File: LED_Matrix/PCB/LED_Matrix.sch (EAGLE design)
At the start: 8 parts, among them U1 ATTINY48, U2 ULN2803AFWG

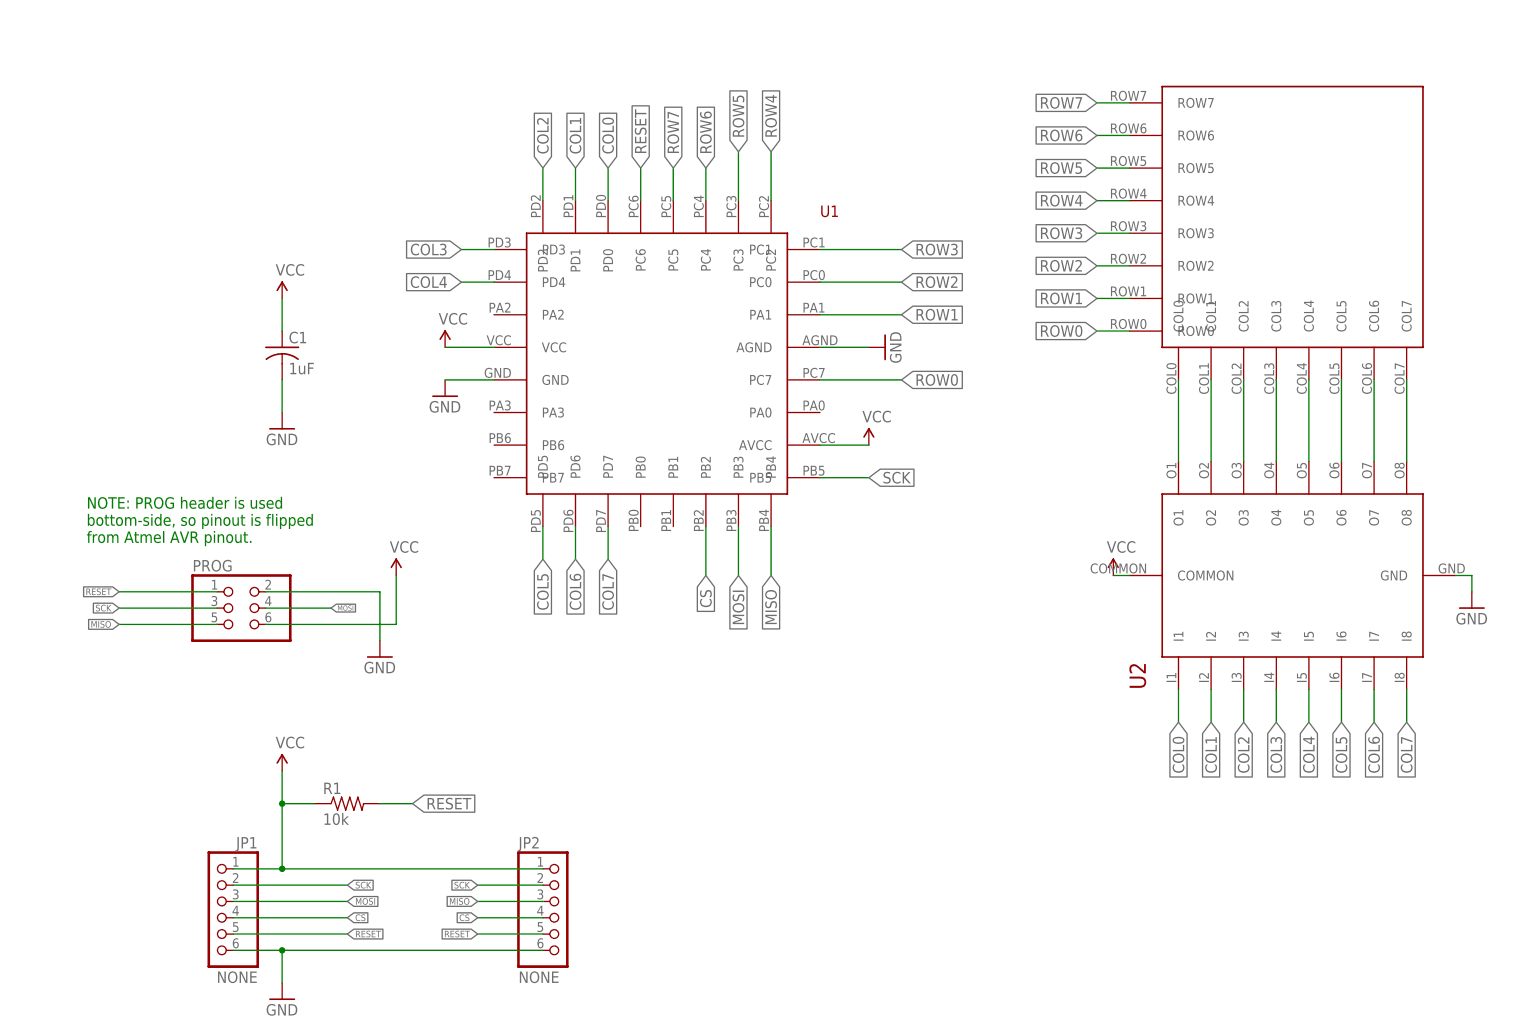
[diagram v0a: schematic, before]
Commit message: matrix - Rev-01b - Adjust size, mouting holes, split matrix connector.  No routing changes.
Dimensionsional, mounting, silkscreen and schematic changes.  (actually - there
was one very minor routing adjustment where a DRC check failed).

Changes:
    - Board was 1260x1260mils: changed to correct 1250x1250, which is the size
      of the LED matrix.
    - Mouting holes where 1010 mils apart, and still would hit the matrix
      headers with #4 screws.  Rather than do the correct 1000mils, went to
      1050 mils, which allow us only of one pair of mounting pins at a time.
      This is good because it allows all boards in a chain to use exactly two
      mounting holes.  Holes are now also labeled on the silkscreen.
    - Split LED matrix connector so that the BOM can have correct reference
      designator linkages.
    - Changed JP1/2 to more correct J/P designations
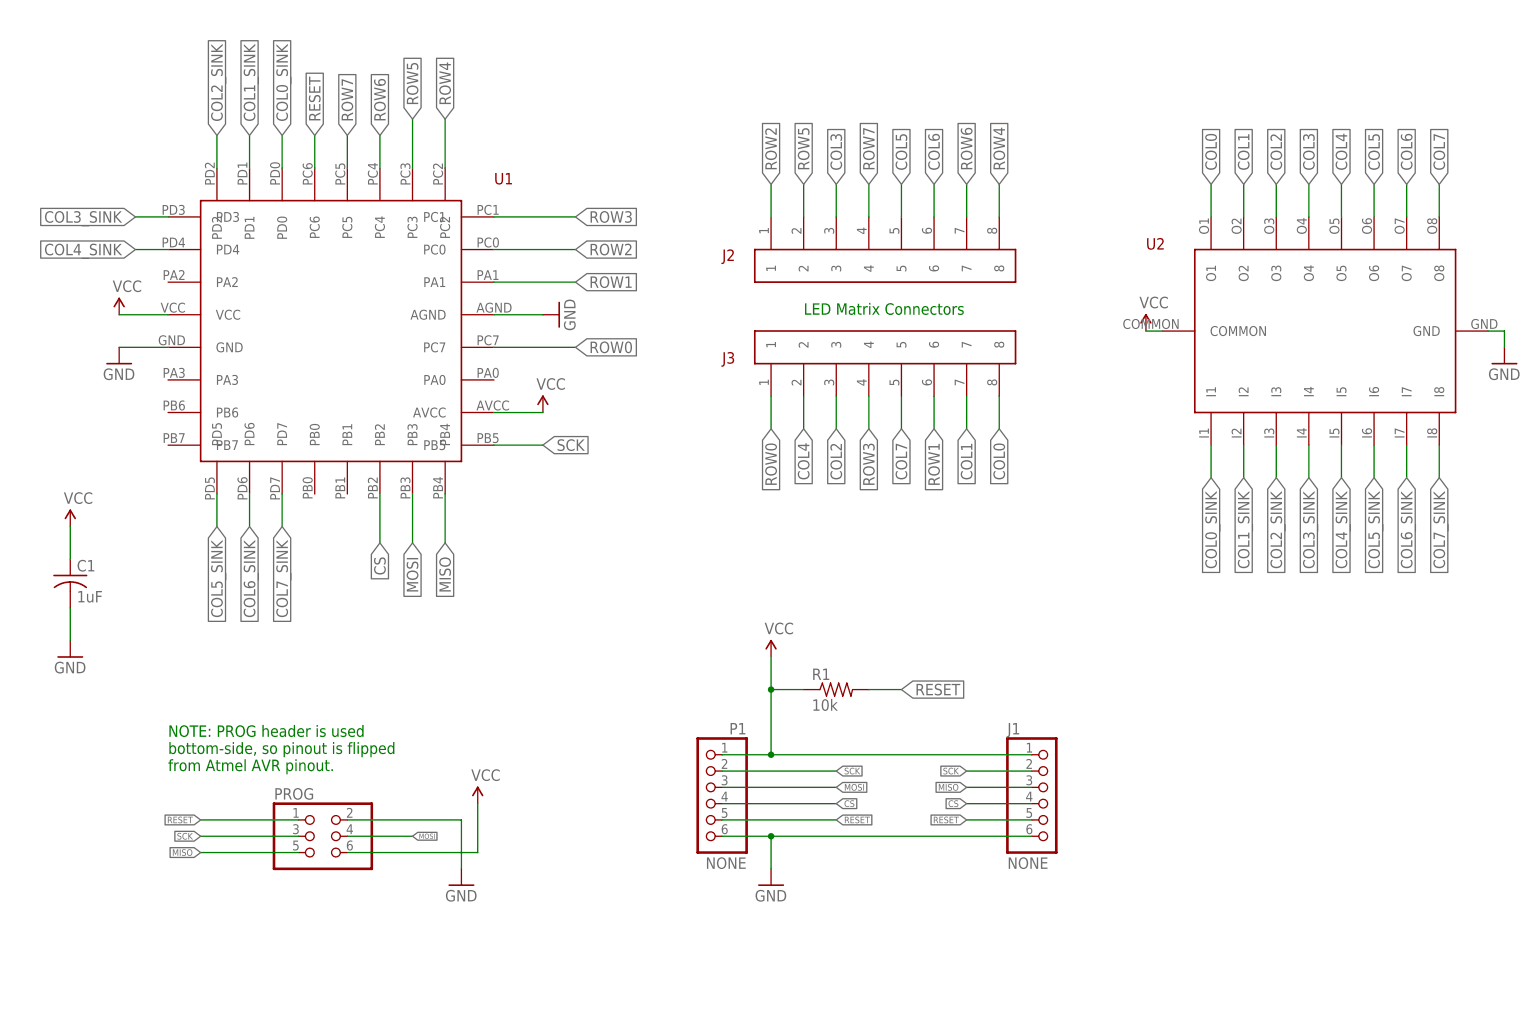
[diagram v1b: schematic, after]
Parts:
- removed JP1, JP2: NONE, LED_Matrix:PINHD-1X6
- removed LEDMATRIX: 8X8_LED_MATRIX, LED_Matrix:8X8_LED_MATRIX
- added J1, P1: NONE, LED_Matrix:PINHD-1X6
- added J2, J3: HEADER-1X8, LED_Matrix:HEADER-1X8
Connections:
- removed net N$1: LEDMATRIX.COL0, U2.O1
- removed net N$2: LEDMATRIX.COL1, U2.O2
- removed net N$3: LEDMATRIX.COL2, U2.O3
- removed net N$4: LEDMATRIX.COL3, U2.O4
- removed net N$5: LEDMATRIX.COL4, U2.O5
- removed net N$6: LEDMATRIX.COL5, U2.O6
- removed net N$7: LEDMATRIX.COL6, U2.O7
- removed net N$8: LEDMATRIX.COL7, U2.O8
- new net COL0_SINK: U1.PD0, U2.I1
- new net COL1_SINK: U1.PD1, U2.I2
- new net COL2_SINK: U1.PD2, U2.I3
- new net COL3_SINK: U1.PD3, U2.I4
- new net COL4_SINK: U1.PD4, U2.I5
- new net COL5_SINK: U1.PD5, U2.I6
- new net COL6_SINK: U1.PD6, U2.I7
- new net COL7_SINK: U1.PD7, U2.I8
- net COL0: now also J3.8, U2.O1; no longer U1.PD0, U2.I1
- net COL1: now also J3.7, U2.O2; no longer U1.PD1, U2.I2
- net COL2: now also J3.3, U2.O3; no longer U1.PD2, U2.I3
- net COL3: now also J2.3, U2.O4; no longer U1.PD3, U2.I4
- net COL4: now also J3.2, U2.O5; no longer U1.PD4, U2.I5
- net COL5: now also J2.5, U2.O6; no longer U1.PD5, U2.I6
- net COL6: now also J2.6, U2.O7; no longer U1.PD6, U2.I7
- net COL7: now also J3.5, U2.O8; no longer U1.PD7, U2.I8
- net CS: now also J1.4, P1.4; no longer JP1.4, JP2.4
- net GND: now also J1.6, P1.6; no longer JP1.6, JP2.6
- net MISO: now also J1.3; no longer JP2.3
- net MOSI: now also P1.3; no longer JP1.3
- net RESET: now also J1.5, P1.5; no longer JP1.5, JP2.5
- net ROW0: now also J3.1; no longer LEDMATRIX.ROW0
- net ROW1: now also J3.6; no longer LEDMATRIX.ROW1
- net ROW2: now also J2.1; no longer LEDMATRIX.ROW2
- net ROW3: now also J3.4; no longer LEDMATRIX.ROW3
- net ROW4: now also J2.8; no longer LEDMATRIX.ROW4
- net ROW5: now also J2.2; no longer LEDMATRIX.ROW5
- net ROW6: now also J2.7; no longer LEDMATRIX.ROW6
- net ROW7: now also J2.4; no longer LEDMATRIX.ROW7
- net SCK: now also J1.2, P1.2; no longer JP1.2, JP2.2
- net VCC: now also J1.1, P1.1; no longer JP1.1, JP2.1
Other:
- note added: "LED Matrix Connectors"
- moved on the sheet: C1, PROG, R1, U1, U2
